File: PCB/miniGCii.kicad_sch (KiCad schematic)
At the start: 3 parts, among them J1 AudioJack4, J2 AudioJack4, J3 Conn_01x05_Pin

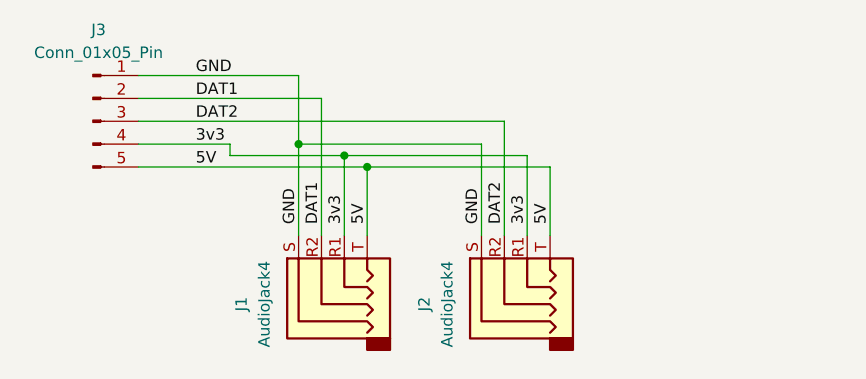
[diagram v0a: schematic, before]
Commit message: Created PCB layout
Signed-off-by: Devnol <pgkoutsoumanis@gmail.com>
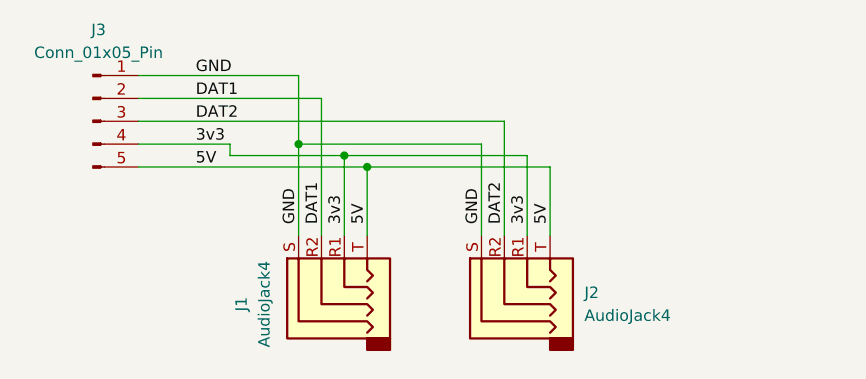
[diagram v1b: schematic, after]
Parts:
- J2: footprint (none) -> Connector_Audio:Jack_3.5mm_KoreanHropartsElec_PJ-320D-4A_Horizontal
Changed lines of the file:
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@@
 		(fields_autoplaced yes)
 		(property "Reference" "J2"
-			(at 64.77 102.87 0)
+			(at 82.55 101.5999 90)
 			(effects
 				(font
 					(size 1.27 1.27)
 				)
+				(justify right)
 			)
 		)
 		(property "Value" "AudioJack4"
-			(at 67.31 102.87 0)
+			(at 82.55 104.1399 90)
 			(effects
 				(font
 					(size 1.27 1.27)
 				)
+				(justify right)
 			)
 		)
-		(property "Footprint" ""
+		(property "Footprint" "Connector_Audio:Jack_3.5mm_KoreanHropartsElec_PJ-320D-4A_Horizontal"
 			(at 73.66 100.33 0)
 			(effects

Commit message: changed connector to 90deg, added fabrication outputs
Signed-off-by: Devnol <pgkoutsoumanis@gmail.com>
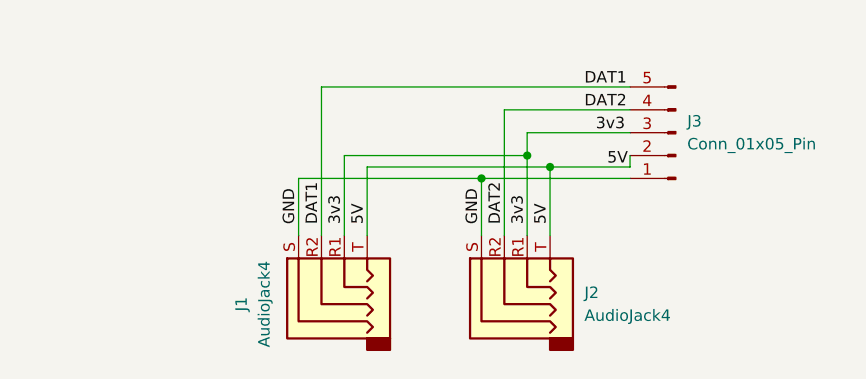
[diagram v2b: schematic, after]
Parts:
- J3: footprint Connector_JST:JST_PH_B5B-PH-K_1x05_P2.00mm_Vertical -> Connector_JST:JST_PH_S5B-PH-K_1x05_P2.00mm_Horizontal
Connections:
- net 3v3: now also J3.3 (Pin_3); no longer J3.4 (Pin_4)
- net 5V: now also J3.2 (Pin_2); no longer J3.5 (Pin_5)
- net DAT1: now also J3.5 (Pin_5); no longer J3.2 (Pin_2)
- net DAT2: now also J3.4 (Pin_4); no longer J3.3 (Pin_3)
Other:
- moved on the sheet: J3
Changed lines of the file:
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@@
 	(paper "A4")
 	(junction
-		(at 50.8 85.09)
+		(at 71.12 88.9)
 		(diameter 0)
 		(color 0 0 0 0)
 	)
 	(junction
-		(at 55.88 86.36)
+		(at 76.2 86.36)
 		(diameter 0)
 		(color 0 0 0 0)
 	)
 	(junction
-		(at 58.42 87.63)
+		(at 78.74 87.63)
 		(diameter 0)
 		(color 0 0 0 0)
@@
 	(wire
 		(pts
-			(xy 71.12 95.25) (xy 71.12 85.09)
-		)
-		(stroke
-			(width 0)
-			(type default)
-		)
-	)
-	(wire
-		(pts
-			(xy 43.18 86.36) (xy 43.18 85.09)
+			(xy 71.12 95.25) (xy 71.12 88.9)
+		)
+		(stroke
+			(width 0)
+			(type default)
+		)
+	)
+	(wire
+		(pts
+			(xy 87.63 81.28) (xy 73.66 81.28)
 		)
 		(stroke
@@
 	(wire
 		(pts
-			(xy 50.8 77.47) (xy 50.8 85.09)
-		)
-		(stroke
-			(width 0)
-			(type default)
-		)
-	)
-	(wire
-		(pts
-			(xy 53.34 80.01) (xy 53.34 95.25)
-		)
-		(stroke
-			(width 0)
-			(type default)
-		)
-	)
-	(wire
-		(pts
-			(xy 43.18 85.09) (xy 33.02 85.09)
-		)
-		(stroke
-			(width 0)
-			(type default)
-		)
-	)
-	(wire
-		(pts
-			(xy 50.8 77.47) (xy 33.02 77.47)
+			(xy 53.34 78.74) (xy 87.63 78.74)
+		)
+		(stroke
+			(width 0)
+			(type default)
+		)
+	)
+	(wire
+		(pts
+			(xy 78.74 87.63) (xy 87.63 87.63)
+		)
+		(stroke
+			(width 0)
+			(type default)
+		)
+	)
+	(wire
+		(pts
+			(xy 76.2 83.82) (xy 87.63 83.82)
+		)
+		(stroke
+			(width 0)
+			(type default)
+		)
+	)
+	(wire
+		(pts
+			(xy 71.12 88.9) (xy 87.63 88.9)
+		)
+		(stroke
+			(width 0)
+			(type default)
+		)
+	)
+	(wire
+		(pts
+			(xy 53.34 78.74) (xy 53.34 95.25)
 		)
 		(stroke
@@
 	(wire
 		(pts
-			(xy 73.66 82.55) (xy 33.02 82.55)
-		)
-		(stroke
-			(width 0)
-			(type default)
-		)
-	)
-	(wire
-		(pts
-			(xy 50.8 85.09) (xy 71.12 85.09)
+			(xy 76.2 83.82) (xy 76.2 86.36)
 		)
 		(stroke
@@
 	(wire
 		(pts
-			(xy 55.88 86.36) (xy 43.18 86.36)
-		)
-		(stroke
-			(width 0)
-			(type default)
-		)
-	)
-	(wire
-		(pts
-			(xy 53.34 80.01) (xy 33.02 80.01)
-		)
-		(stroke
-			(width 0)
-			(type default)
-		)
-	)
-	(wire
-		(pts
-			(xy 50.8 95.25) (xy 50.8 85.09)
-		)
-		(stroke
-			(width 0)
-			(type default)
-		)
-	)
-	(wire
-		(pts
-			(xy 73.66 82.55) (xy 73.66 95.25)
+			(xy 50.8 88.9) (xy 71.12 88.9)
+		)
+		(stroke
+			(width 0)
+			(type default)
+		)
+	)
+	(wire
+		(pts
+			(xy 87.63 87.63) (xy 87.63 86.36)
+		)
+		(stroke
+			(width 0)
+			(type default)
+		)
+	)
+	(wire
+		(pts
+			(xy 50.8 95.25) (xy 50.8 88.9)
+		)
+		(stroke
+			(width 0)
+			(type default)
+		)
+	)
+	(wire
+		(pts
+			(xy 73.66 81.28) (xy 73.66 95.25)
 		)
 		(stroke
@@
 		(pts
 			(xy 58.42 95.25) (xy 58.42 87.63)
-		)
-		(stroke
-			(width 0)
-			(type default)
-		)
-	)
-	(wire
-		(pts
-			(xy 33.02 87.63) (xy 58.42 87.63)
 		)
 		(stroke
@@
 	)
 	(label "3v3"
-		(at 39.37 85.09 0)
+		(at 83.82 83.82 0)
 		(fields_autoplaced yes)
 		(effects
@@
 	)
 	(label "DAT2"
-		(at 39.37 82.55 0)
-		(fields_autoplaced yes)
-		(effects
-			(font
-				(size 1.27 1.27)
-			)
-			(justify left bottom)
-		)
-	)
-	(label "GND"
-		(at 39.37 77.47 0)
+		(at 82.55 81.28 0)
 		(fields_autoplaced yes)
 		(effects
@@
 	)
 	(label "5V"
-		(at 39.37 87.63 0)
+		(at 85.09 87.63 0)
 		(fields_autoplaced yes)
 		(effects
@@
 	)
 	(label "DAT1"
-		(at 39.37 80.01 0)
+		(at 82.55 78.74 0)
 		(fields_autoplaced yes)
 		(effects
@@
 	(symbol
 		(lib_id "Connector:Conn_01x05_Pin")
-		(at 27.94 82.55 0)
+		(at 92.71 83.82 180)
 		(unit 1)
 		(exclude_from_sim no)
@@
 		(fields_autoplaced yes)
 		(property "Reference" "J3"
-			(at 28.575 72.39 0)
+			(at 93.98 82.5499 0)
 			(effects
 				(font
 					(size 1.27 1.27)
 				)
+				(justify right)
 			)
 		)
 		(property "Value" "Conn_01x05_Pin"
-			(at 28.575 74.93 0)
+			(at 93.98 85.0899 0)
 			(effects
 				(font
 					(size 1.27 1.27)
 				)
-			)
-		)
-		(property "Footprint" "Connector_JST:JST_PH_B5B-PH-K_1x05_P2.00mm_Vertical"
-			(at 27.94 82.55 0)
+				(justify right)
+			)
+		)
+		(property "Footprint" "Connector_JST:JST_PH_S5B-PH-K_1x05_P2.00mm_Horizontal"
+			(at 92.71 83.82 0)
 			(effects
 				(font
@@
 		)
 		(property "Datasheet" "~"
-			(at 27.94 82.55 0)
+			(at 92.71 83.82 0)
 			(effects
 				(font
@@
 		)
 		(property "Description" "Generic connector, single row, 01x05, script generated"
-			(at 27.94 82.55 0)
-			(effects
-				(font
+			(at 92.71 83.82 0)
+			(effects
+				(font
